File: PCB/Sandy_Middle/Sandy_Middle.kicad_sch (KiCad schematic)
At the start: 72 parts, among them J1 Conn_02x02_Top_Bottom, J2 Conn_02x02_Top_Bottom, J3 Conn_02x02_Top_Bottom

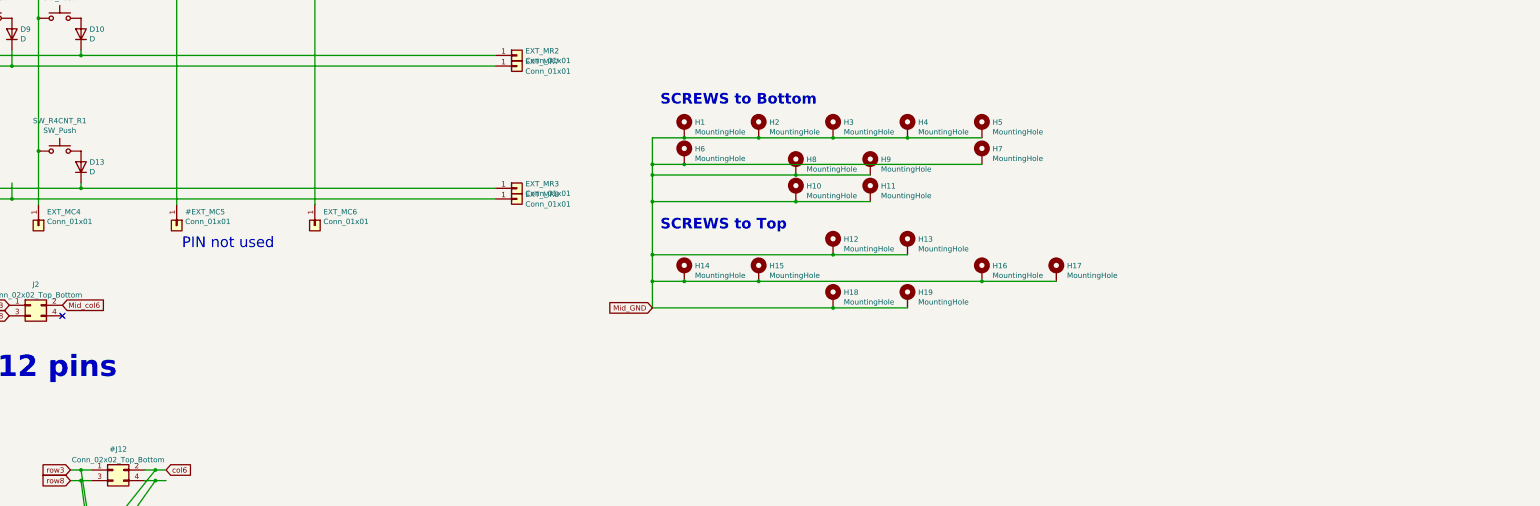
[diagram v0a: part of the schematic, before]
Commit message: WIP ネジ穴位置、スイッチ位置調整中
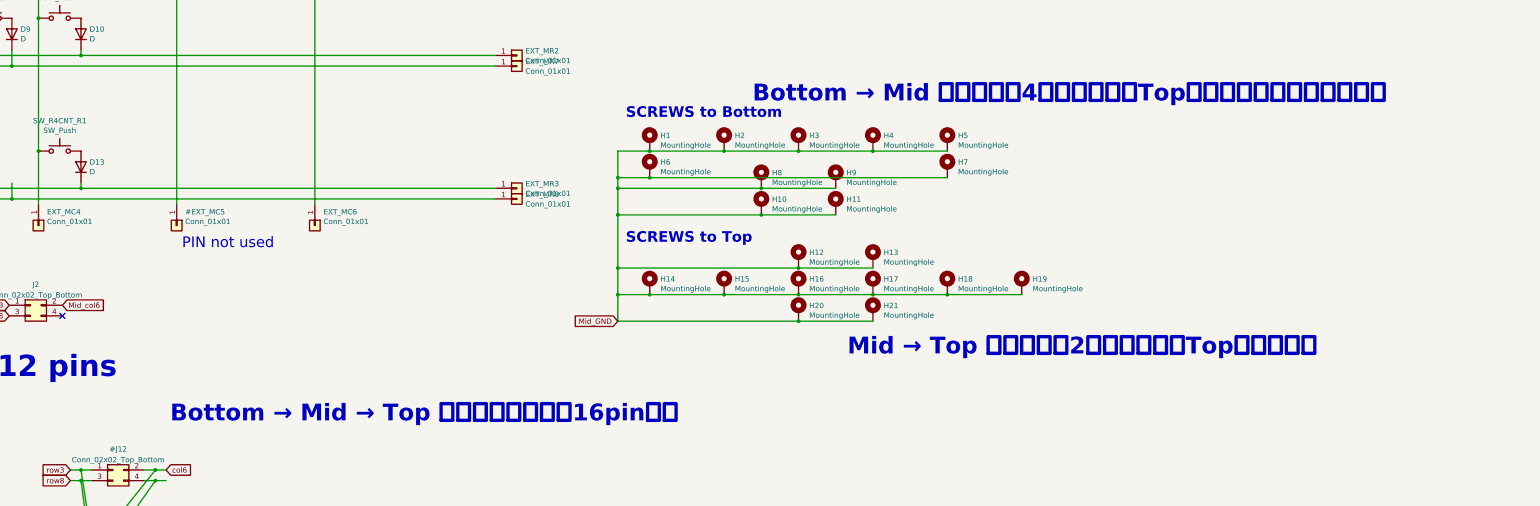
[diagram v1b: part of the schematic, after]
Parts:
- added H20, H21: MountingHole, locallib:MountingHole_2.2mm_M2_Pad_minimal, symbol Mechanical:MountingHole_Pad
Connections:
- net Mid_GND: now also H20.1, H21.1
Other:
- note added: "Bottom → Mid → Top を繋ぐためには、16pin必要"
- note added: "Bottom → Mid にネジ穴を4個追すれば、Topへ繋げる可能性が出てくる"
- note added: "Mid → Top にネジ穴を2個追すれば、Topまで繋がる"
- moved on the sheet: H1, H10, H11, H12, H13, H14, H15, H16, H17, H18, H19, H2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

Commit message: WIP ネジ穴位置、スイッチ位置調整中
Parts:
- SW_BS1, SW_TAB1: footprint MX_Alps_Hybrid:MXOnly-1.5U-Hotswap-guide -> MX_Alps_Hybrid:MXOnly-1U-Hotswap-guide
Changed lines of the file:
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@@
 			)
 		)
-		(property "Footprint" "MX_Alps_Hybrid:MXOnly-1.5U-Hotswap-guide"
+		(property "Footprint" "MX_Alps_Hybrid:MXOnly-1U-Hotswap-guide"
 			(at 257.81 69.85 0)
 			(effects
@@
 			)
 		)
-		(property "Footprint" "MX_Alps_Hybrid:MXOnly-1.5U-Hotswap-guide"
+		(property "Footprint" "MX_Alps_Hybrid:MXOnly-1U-Hotswap-guide"
 			(at 43.18 69.85 0)
 			(effects

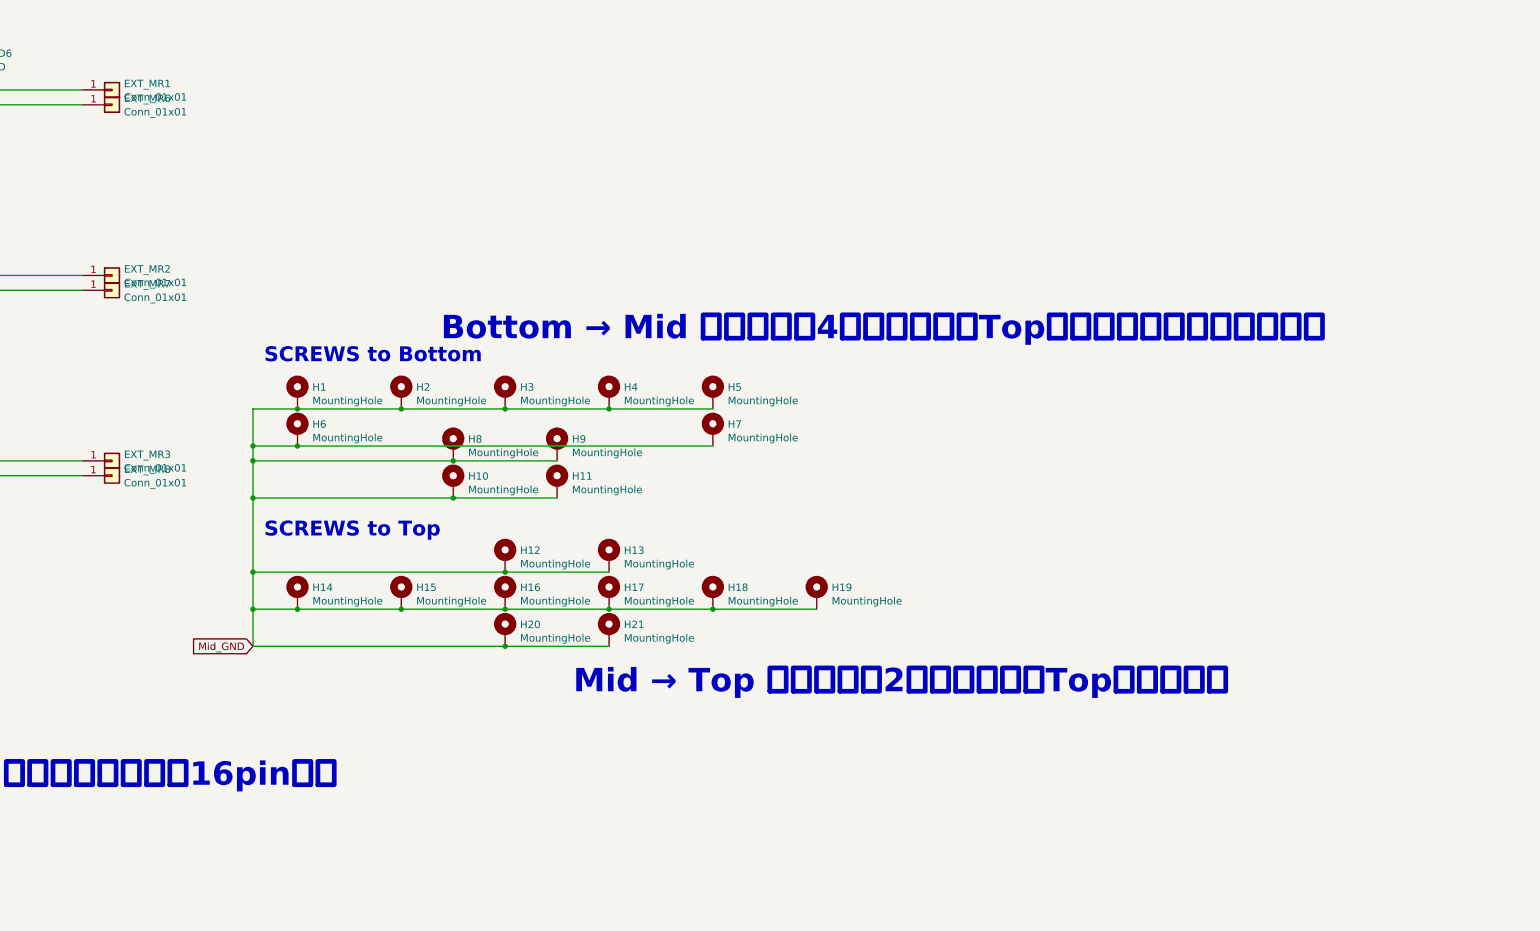
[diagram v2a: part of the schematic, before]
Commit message: Mid→Topのネジ穴を追加して配置
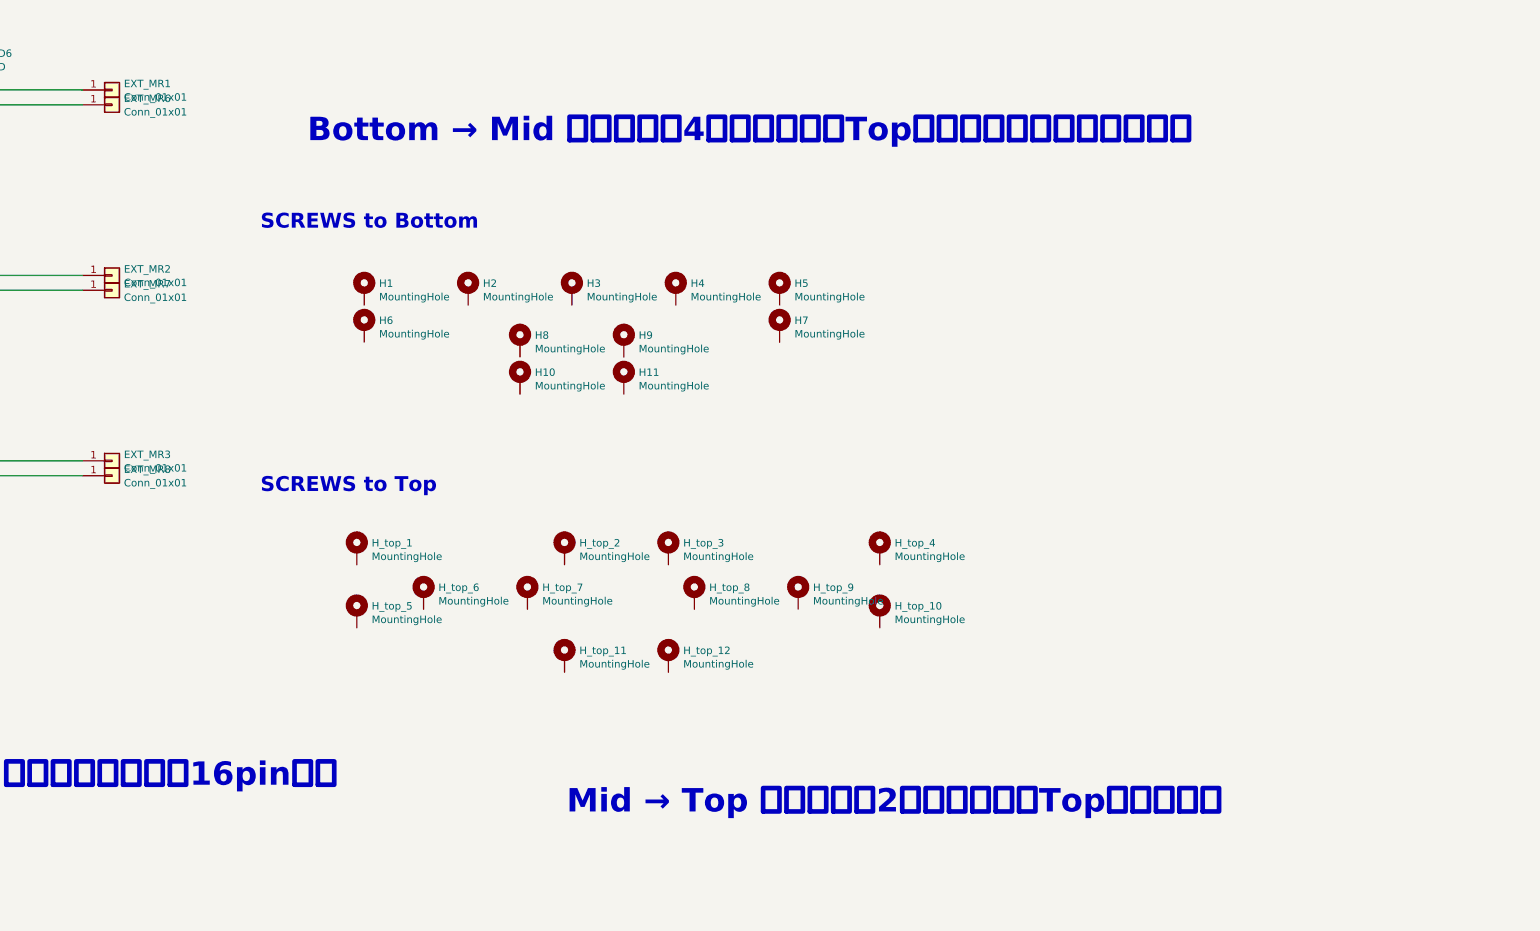
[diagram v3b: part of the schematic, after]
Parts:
- added H_top_11, H_top_12: MountingHole, locallib:MountingHole_2.2mm_M2_Pad_minimal, symbol Mechanical:MountingHole_Pad
- renumbered H14 to H_top_1, H21 to H_top_10, H12 to H_top_2, H13 to H_top_3, H20 to H_top_4, H15 to H_top_5, H16 to H_top_6, H17 to H_top_7, H18 to H_top_8, H19 to H_top_9
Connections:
- net Mid_GND: no longer H1.1, H10.1, H11.1, H2.1, H3.1, H4.1, H5.1, H6.1, H7.1, H8.1, H9.1, H_top_1.1, H_top_10.1, H_top_2.1, H_top_3.1, H_top_4.1, H_top_5.1, H_top_6.1, H_top_7.1, H_top_8.1, H_top_9.1
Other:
- moved on the sheet: H1, H10, H11, H2, H3, H4, H5, H6, H7, H8, H9, H_top_1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

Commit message: Mid→Baseのネジ穴を追加して配置
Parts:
- added H10, H2, H5, H6, H9: MountingHole, locallib:MountingHole_2.2mm_M2_Pad_minimal, symbol Mechanical:MountingHole_Pad
- renumbered H6 to H11, H7 to H12, H8 to H13, H9 to H14, H10 to H15, H11 to H16, H2 to H7, H5 to H8
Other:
- note added: "Bottom → Mid は、12pin（6row + 5col + GND)必要。 Bottom → Mid → Top を繋ぐためには、16pin必要（12pin + 2row + 2col)。"
- note removed: "Bottom to Mid: require 12 pins"
- note removed: "Bottom to Mid: require 16 pins Mid to Top: require 12 pins"
- note removed: "Bottom → Mid → Top を繋ぐためには、16pin必要"
- note removed: "Bottom → Mid にネジ穴を4個追すれば、Topへ繋げる可能性が出てくる"
- note removed: "Mid → Top にネジ穴を2個追すれば、Topまで繋がる"
- moved on the sheet: H11, H12, H13, H14, H15, H16, H7, H8

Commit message: ネジ穴と接続するピンを調整中
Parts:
- removed D10, D8: D, locallib:D_SOD-123_Emphasized_Direction_Line, symbol Device:D
- removed SW_;1, SW_H1: SW_Push, MX_Alps_Hybrid:MXOnly-1U-Hotswap-guide, symbol Switch:SW_Push
- added EXT_MC1, EXT_MC5, EXT_MR0, EXT_MR5: Conn_01x01, TestPoint:TestPoint_THTPad_D2.0mm_Drill1.0mm, symbol Connector_Generic:Conn_01x01
- added H_top_13: MountingHole, locallib:MountingHole_2.2mm_M2_Pad_minimal, symbol Mechanical:MountingHole_Pad
- renumbered SW_'1 to SW_H1
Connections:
- net Mid_col1: now also EXT_MC1.1 (Pin_1)
- net Mid_col5: now also EXT_MC5.1 (Pin_1)
- net Mid_row0: now also EXT_MR0.1 (Pin_1)
- net Mid_row5: now also EXT_MR5.1 (Pin_1)
- net Top_GND: now also H_top_13.1
- net Top_col0: now also H_top_1.1
- net Top_col1: now also H_top_6.1
- net Top_col2: now also H_top_2.1
- net Top_col3: now also H_top_11.1
- net Top_col4: now also H_top_3.1
- net Top_col5: now also H_top_9.1
- net Top_col6: now also H_top_4.1
- net Top_row0: now also H_top_5.1
- net Top_row1: now also H_top_7.1
- net Top_row5: now also H_top_10.1
- net Top_row6: now also H_top_8.1
- net Top_row2: now reaches H_top_12.1
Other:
- note added: "SW_H1は、本来 Col4 → Row2 に配置されるが、 Top基板への接続本数を減らすため、隣へ移動。"
- moved on the sheet: H1, H10, H11, H12, H13, H14, H15, H16, H3, H4, H5, H6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

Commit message: ネジ穴と接続するピンを調整中
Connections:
- net Top_row2 is gone; now on net Mid_row6: H_top_12.1
- net Mid_GND: now also H12.1, H_top_10.1
- net Mid_col0: now also H1.1, H_top_1.1
- net Mid_col1: now also H9.1, H_top_6.1
- net Mid_col2: now also H7.1, H_top_7.1
- net Mid_col3: now also H3.1, H_top_2.1
- net Mid_col4: now also H4.1, H_top_3.1
- net Mid_col5: now also H8.1, H_top_8.1
- net Mid_col6: now also H6.1, H_top_4.1
- net Mid_row0: now also H11.1, H_top_5.1
- net Mid_row1: now also H2.1, H_top_11.1
- net Mid_row2: now also H13.1, H_top_13.1
- net Mid_row3: now also H15.1
- net Mid_row5: now also H10.1, H_top_9.1
- net Mid_row6: now also H5.1
- net Mid_row7: now also H14.1
- net Mid_row8: now also H16.1
- net Top_GND: no longer H_top_13.1
- net Top_col0: no longer H_top_1.1
- net Top_col1: no longer H_top_6.1
- net Top_col2: no longer H_top_2.1
- net Top_col3: no longer H_top_11.1
- net Top_col4: no longer H_top_3.1
- net Top_col5: no longer H_top_9.1
- net Top_col6: no longer H_top_4.1
- net Top_row0: no longer H_top_5.1
- net Top_row1: no longer H_top_7.1
- net Top_row5: no longer H_top_10.1
- net Top_row6: no longer H_top_8.1
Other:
- note added: "Mid は、12pin（6row + 5col + GND）、 Top は、13pin（5row + 7col + GND）必要。 Bottom → Mid → Top を繋ぐためには、 Midで使わないピンも含めて16pin必要。"
- note removed: "Bottom → Mid は、12pin（6row + 5col + GND)必要。 Bottom → Mid → Top を繋ぐためには、16pin必要（12pin + 2row + 2col)。"
- moved on the sheet: H1, H10, H11, H12, H13, H14, H15, H16, H2, H3, H4, H5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

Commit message: ネジ位置調整
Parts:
- SW_BS1: footprint MX_Alps_Hybrid:MXOnly-1U-Hotswap-guide -> MX_Alps_Hybrid:MXOnly-1U-Hotswap-screw-hole-side1-guide
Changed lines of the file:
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@@
 			)
 		)
-		(property "Footprint" "MX_Alps_Hybrid:MXOnly-1U-Hotswap-guide"
+		(property "Footprint" "MX_Alps_Hybrid:MXOnly-1U-Hotswap-screw-hole-side1-guide"
 			(at 257.81 69.85 0)
 			(effects

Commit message: JST SH コネクタのフットプリントにコートヤードを追加
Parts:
- J1, J2, J3: footprint locallib:JST_SH_SM04B-SRSS-TB_1x04-1MP_P1.00mm_Horizontal_wCable_housing_spare_pin -> locallib:JST_SH_SM04B-SRSS-TB_1x04-1MP_P1.00mm_Horizontal_wCable_housing_spare_pin_courtyard
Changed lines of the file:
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@@
 			)
 		)
-		(property "Footprint" "locallib:JST_SH_SM04B-SRSS-TB_1x04-1MP_P1.00mm_Horizontal_wCable_housing_spare_pin"
+		(property "Footprint" "locallib:JST_SH_SM04B-SRSS-TB_1x04-1MP_P1.00mm_Horizontal_wCable_housing_spare_pin_courtyard"
 			(at 168.275 175.26 0)
 			(effects
@@
 			)
 		)
-		(property "Footprint" "locallib:JST_SH_SM04B-SRSS-TB_1x04-1MP_P1.00mm_Horizontal_wCable_housing_spare_pin"
+		(property "Footprint" "locallib:JST_SH_SM04B-SRSS-TB_1x04-1MP_P1.00mm_Horizontal_wCable_housing_spare_pin_courtyard"
 			(at 125.095 175.26 0)
 			(effects
@@
 			)
 		)
-		(property "Footprint" "locallib:JST_SH_SM04B-SRSS-TB_1x04-1MP_P1.00mm_Horizontal_wCable_housing_spare_pin"
+		(property "Footprint" "locallib:JST_SH_SM04B-SRSS-TB_1x04-1MP_P1.00mm_Horizontal_wCable_housing_spare_pin_courtyard"
 			(at 81.915 175.26 0)
 			(effects
